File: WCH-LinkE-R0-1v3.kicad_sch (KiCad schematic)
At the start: 29 parts, among them Q1 IRLML2502TRPBF, Q2 IRLML2502TRPBF, SW1 PTS636_SL43_SMTR_LFS, SW2 PTS636_SL43_SMTR_LFS, SW3 PTS636_SL43_SMTR_LFS, U4 CH32V305FBP6, Y1 Crystal_GND24

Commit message: Improve layout
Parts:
- Q1, Q2: footprint Package_TO_SOT_SMD:SOT-23 -> Tiny_Scarab:SOT-23
- renumbered C13 to C12, C12 to C13, C14 to C15, C14 to C18, C14 to C19, D5 to D4, D4 to D5, R13 to R11, R13 to R14, R16 to R15, R11 to R16, R2 to R17, R3 to R18, R2 to R19, R1 to R20, R13 to R4, R14 to R5, R15 to R6, R8 to R7
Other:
- note added: "Mode LEDs"
- note added: "RST and IAP Buttons"
- note added: "The CH32V305FBP6 MCU outputs the LED_CON signal to indicate if it works in ARM-mode or RISC-V-mode."
- note added: "The RST button resets the CH32V305FBP6 MCU, the IAP button brings it into IAP mode."
- note removed: "The USB4110-GF-A USB-C connector only provides the basic USB2.0 data signals. We fuse the incoming VBUS supply at 1A."
- moved on the sheet: C14, C15, D4, D5, R15, R16, R17, R18, R19, R20, SW2, SW3

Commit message: Improve layout
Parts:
- added C18: 10u, Capacitor_SMD:C_0805_2012Metric, symbol Device:C
- added C21: 100n, Capacitor_SMD:C_0402_1005Metric_Pad0.74x0.62mm_HandSolder, symbol Device:C
- added R5, R7: 0, Resistor_SMD:R_0402_1005Metric_Pad0.72x0.64mm_HandSolder, symbol Device:R
- C19: renamed from C18; GPN GPC0402104-25 -> (none); MPN (none) -> GPC0402104-25
- C20: renamed from C19; GPN GPC0402104-25 -> (none); MPN (none) -> GPC0402104-25
- C22: renamed from C14; GPN GPC0402104-25 -> (none); MPN (none) -> GPC0402104-25
- C23: renamed from C15; GPN GPC0402104-25 -> (none); MPN (none) -> GPC0402104-25
- C24: renamed from C12; GPN GPC0402220 -> (none); MPN (none) -> GPC0402220; now left out of the parts list
- C25: renamed from C13; GPN GPC0402220 -> (none); MPN (none) -> GPC0402220; now left out of the parts list
- LED2: renamed from D4; MPN 150060GS55040 -> 150060YS55040; SPN 732-12014-2-ND -> 732-12018-2-ND
- LED3: renamed from D5; MPN 150060GS55040 -> 150060BS55040; SPN 732-12014-2-ND -> 732-12013-2-ND
- Q1, Q2: DPN IRLML2502TRPBFTR-ND -> (none); Distributor DigiKey -> (none); SPN (none) -> IRLML2502TRPBFTR-ND; Supplier (none) -> DigiKey
- R10: renamed from R14; GPN GPR04021K -> (none); MPN (none) -> GPR04021K
- R11: renamed from R17; GPN GPR0402100K -> (none); MPN (none) -> GPR0402100K
- R12: renamed from R18; GPN GPR04021K -> (none); MPN (none) -> GPR04021K
- R13: renamed from R19; value 300 -> 130; GPN GPR0402300R -> (none); MPN (none) -> GPR0402130R
- R14: renamed from R20; value 75 -> 20; GPN GPR040275R -> (none); MPN (none) -> GPR040220R
- R15, R16: GPN GPR040210K -> (none); MPN (none) -> GPR040210K
- R17: renamed from R6; GPN GPR04020R -> (none); MPN (none) -> GPR04020R
- R18: renamed from R4; GPN GPR04020R -> (none); MPN (none) -> GPR04020R
- R19: renamed from R5; GPN GPR04020R -> (none); MPN (none) -> GPR04020R
- R4: renamed from R9; GPN GPR0402270R -> (none); MPN (none) -> GPR0402270R
- R6: renamed from R10; GPN GPR0402270R -> (none); MPN (none) -> GPR0402270R
- R8: renamed from R11; GPN GPR04020R -> (none); MPN (none) -> GPR04020R
- R9: renamed from R7; GPN GPR0402100R -> (none); MPN (none) -> GPR0402100R; now left out of the parts list
- U2: renamed from U4; now not fitted; now left out of the parts list
- renumbered SW2 to SW1, SW3 to SW2, SW1 to SW3, Y1 to XTAL1
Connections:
- net +3V3: now also C18.1, C21.1
- net GND: now also C18.2, C21.2
- net UART3_RX: now also R7.2; no longer U2.4 (PB11)
- net UART3_TX: now also R5.2; no longer U2.3 (PB10)
- new net: R5.1, U2.3 (PB10)
- new net: R7.1, U2.4 (PB11)
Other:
- note added: "10mA 1V95 YELLOW"
- note added: "10mA 3V10 BLUE"
- note removed: "5mA 1V7 AMBER"
- note removed: "5mA 2V9 BLUE"
- moved on the sheet: C19, C20, R4, R6, R8

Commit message: Update design
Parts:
- R5, R7: value 0 -> 270; MPN GPR02010R -> GPR0402270R; now not fitted; now left out of the parts list
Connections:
- net RX: now also R7.1
- net TX: now also R5.1
- net at U2.3 (PB10): now also R4.2, R7.2; no longer R5.1
- net at U2.4 (PB11): now also R5.2, R6.2; no longer R7.1
- removed net UART3_RX: R6.2, R7.2
- removed net UART3_TX: R4.2, R5.2
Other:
- moved on the sheet: R4, R6, R8

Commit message: Update layout
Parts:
- LED2, LED3: value LED -> ~
- Q1, Q2: value IRLML2502TRPBF -> ~
- SW2, SW3: value PTS636_SL43_SMTR_LFS -> ~
- U2: value CH32V305FBP6 -> ~; MPN (none) -> CH32V305FBP6; Manufacturer (none) -> WCH; SPN (none) -> 1005004329064488; Supplier (none) -> AliExpress; now fitted; now in the parts list
- XTAL1: value Crystal_GND24 -> (none)
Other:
- note added: "The CH32V305FBP6 is the heart of the WCH-LinkE-R0-1v3 on-board probe. It must be flashed through signals SWDIO_IN, SWDIO_IN and RST_IN. From then onwards, it gets its instructions from the USB signals USB_N and USB_P. It outputs the following signals to flash and debug the target MCU: - SWDIO_OUT - RST_OUT - TX - RX Note: Resistor R9 must be mounted after flashing the CH32V305FBP6 MCU."
- note removed: "The CH32V305FBP6 is the heart of the WCH-LinkE-R0-1v3 on-board probe. It must be flashed through signals SWDIO_IN, SWDIO_IN and RST_IN. From then onwards, it gets its instructions from the USB signals USB_N and USB_P. It outputs the following signals to flash and debug the target MCU: - SWDIO_OUT - RST_OUT - TX - RX Note: Resistor R7 must be mounted after flashing the CH32V305FBP6 MCU."
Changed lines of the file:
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@@
     (effects (font (size 1.27 1.27)) (justify left bottom))
   )
-  (text "The CH32V305FBP6 is the heart of the WCH-LinkE-R0-1v3\non-board probe. It must be flashed through signals\nSWDIO_IN, SWDIO_IN and RST_IN.\n\nFrom then onwards, it gets its instructions from the USB\nsignals USB_N and USB_P.\n\nIt outputs the following signals to flash and debug the\ntarget MCU:\n- SWDIO_OUT\n- RST_OUT\n- TX\n- RX\n\nNote: Resistor R7 must be mounted after\nflashing the CH32V305FBP6 MCU."
+  (text "The CH32V305FBP6 is the heart of the WCH-LinkE-R0-1v3\non-board probe. It must be flashed through signals\nSWDIO_IN, SWDIO_IN and RST_IN.\n\nFrom then onwards, it gets its instructions from the USB\nsignals USB_N and USB_P.\n\nIt outputs the following signals to flash and debug the\ntarget MCU:\n- SWDIO_OUT\n- RST_OUT\n- TX\n- RX\n\nNote: Resistor R9 must be mounted after\nflashing the CH32V305FBP6 MCU."
     (at 58.42 57.15 0)
     (effects (font (size 1.27 1.27)) (justify left bottom))
@@
       (effects (font (size 1.27 1.27)) (justify left))
     )
-    (property "Value" "IRLML2502TRPBF" (at 55.88 114.3 0)
+    (property "Value" "~" (at 55.88 114.3 0)
       (effects (font (size 1.27 1.27)) (justify left) hide)
     )
@@
       (effects (font (size 1.27 1.27)) (justify right))
     )
-    (property "Value" "LED" (at 43.18 95.25 90)
+    (property "Value" "~" (at 43.18 95.25 90)
       (effects (font (size 1.27 1.27)) (justify right) hide)
     )
@@
       (effects (font (size 1.27 1.27)) (justify left))
     )
-    (property "Value" "PTS636_SL43_SMTR_LFS" (at 113.03 90.17 0)
+    (property "Value" "~" (at 113.03 90.17 0)
       (effects (font (size 1.27 1.27)) hide)
     )
@@
       (effects (font (size 1.27 1.27)) (justify right))
     )
-    (property "Value" "LED" (at 55.88 95.25 0)
+    (property "Value" "~" (at 55.88 95.25 0)
       (effects (font (size 1.27 1.27)) (justify right) hide)
     )
@@
   )
   (symbol (lib_id "Tiny_Scarab:CH32V305FBP6") (at 171.45 39.37 0) (unit 1)
-    (in_bom no) (on_board yes) (dnp yes)
+    (in_bom yes) (on_board yes) (dnp no)
     (property "Reference" "U2" (at 180.34 22.86 0)
       (effects (font (size 1.27 1.27)))
     )
-    (property "Value" "CH32V305FBP6" (at 168.91 22.86 0)
-      (effects (font (size 1.27 1.27)))
+    (property "Value" "~" (at 168.91 22.86 0)
+      (effects (font (size 1.27 1.27)) hide)
     )
     (property "Footprint" "Package_SO:TSSOP-20_4.4x6.5mm_P0.65mm" (at 172.72 69.85 0)
@@
     )
     (property "Datasheet" "" (at 175.26 50.8 0)
+      (effects (font (size 1.27 1.27)) hide)
+    )
+    (property "Manufacturer" "WCH" (at 171.45 39.37 0)
+      (effects (font (size 1.27 1.27)) hide)
+    )
+    (property "MPN" "CH32V305FBP6" (at 168.91 22.86 0)
+      (effects (font (size 1.27 1.27)))
+    )
+    (property "Supplier" "AliExpress" (at 171.45 39.37 0)
+      (effects (font (size 1.27 1.27)) hide)
+    )
+    (property "SPN" "1005004329064488" (at 171.45 39.37 0)
       (effects (font (size 1.27 1.27)) hide)
     )
@@
       (effects (font (size 1.27 1.27)) (justify left))
     )
-    (property "Value" "PTS636_SL43_SMTR_LFS" (at 157.48 91.44 0)
+    (property "Value" "~" (at 157.48 91.44 0)
       (effects (font (size 1.27 1.27)) hide)
     )
@@
       (effects (font (size 1.27 1.27)))
     )
-    (property "Value" "Crystal_GND24" (at 146.05 95.25 90)
+    (property "Value" "" (at 146.05 95.25 90)
       (effects (font (size 1.27 1.27)) hide)
     )
@@
       (effects (font (size 1.27 1.27)) (justify left))
     )
-    (property "Value" "IRLML2502TRPBF" (at 44.45 114.3 0)
+    (property "Value" "~" (at 44.45 114.3 0)
       (effects (font (size 1.27 1.27)) (justify left) hide)
     )

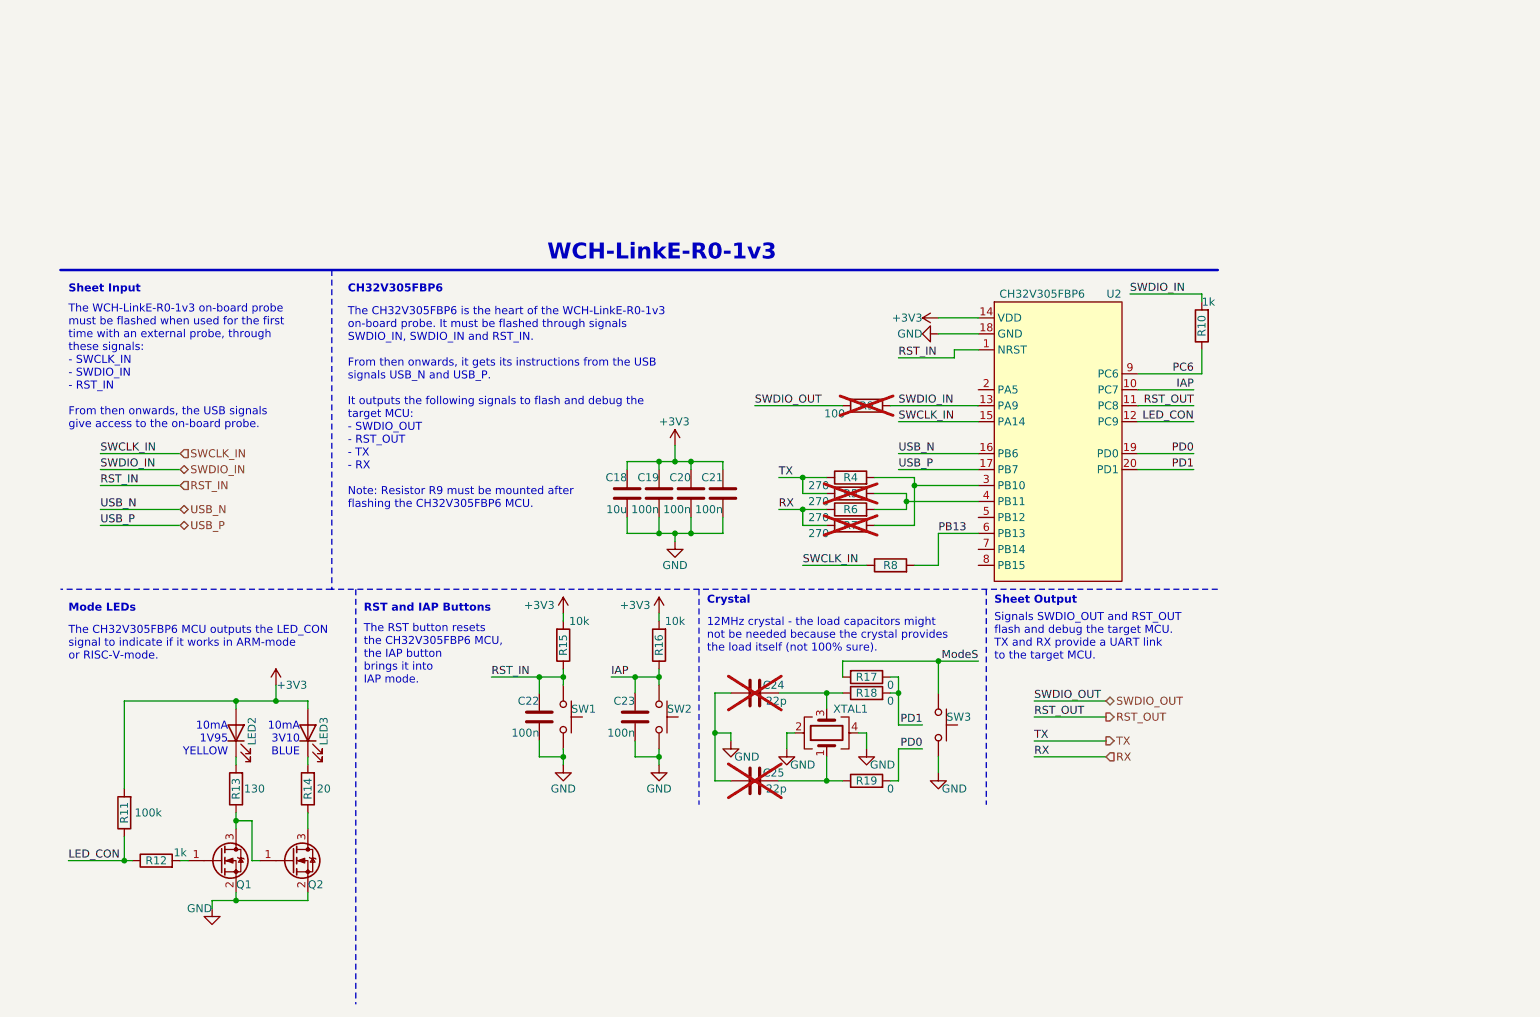
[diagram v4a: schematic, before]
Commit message: Prepare PCB for JLCPCB production
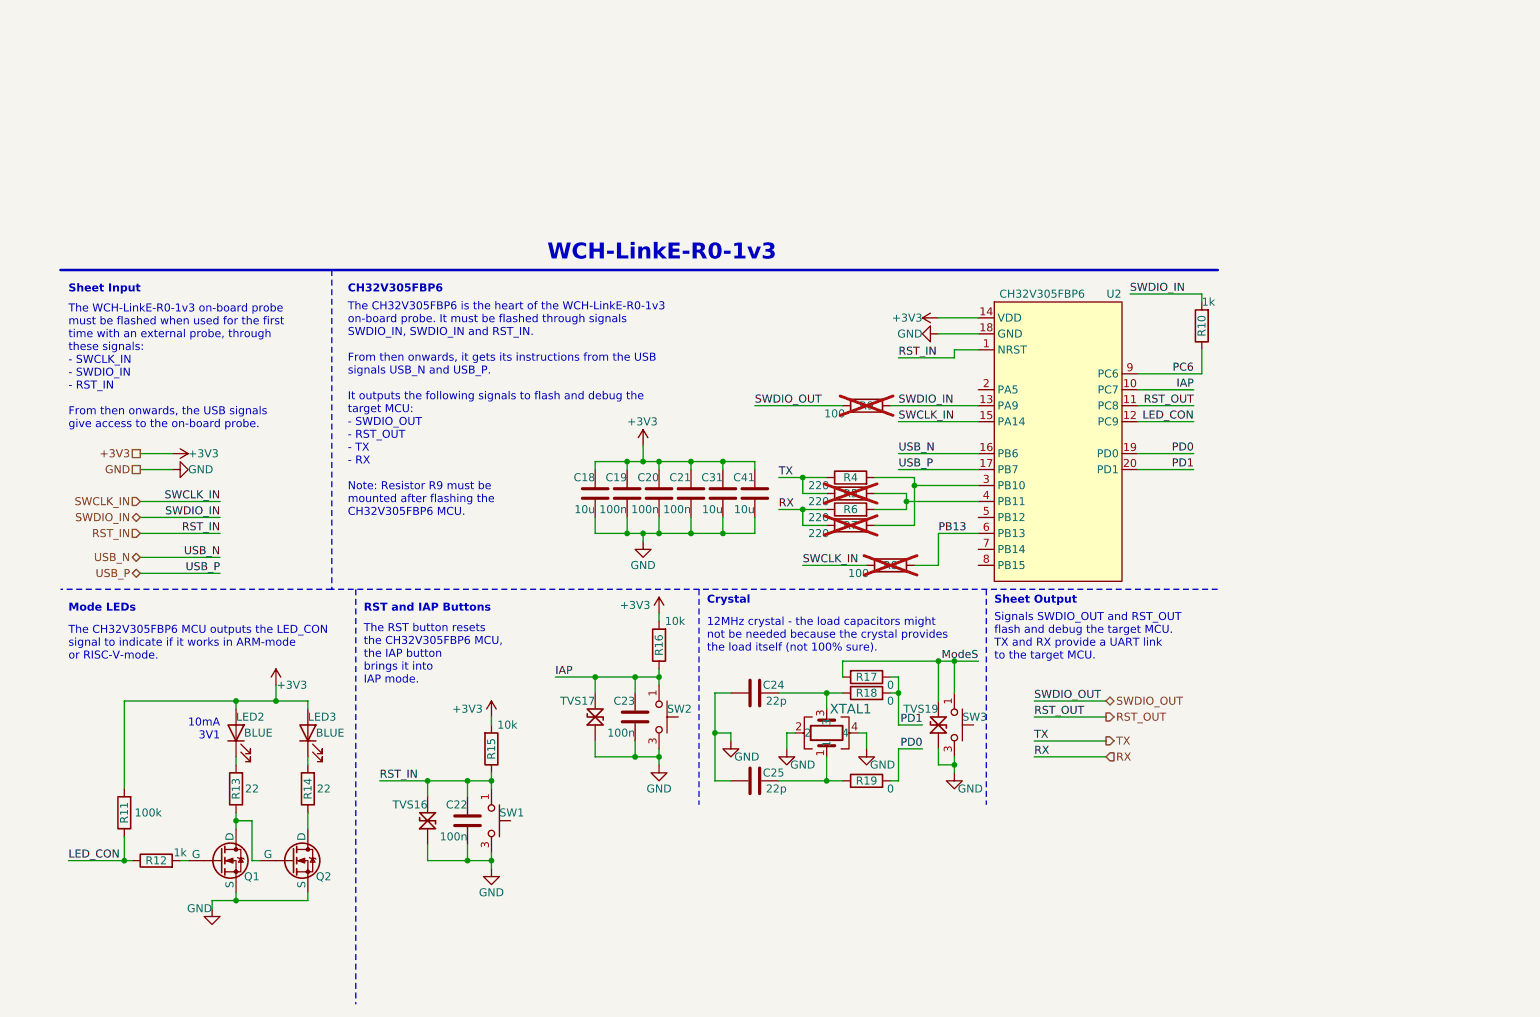
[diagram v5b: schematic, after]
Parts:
- removed LED2, LED3: ~, LED_SMD:LED_0603_1608Metric_Pad1.05x0.95mm_HandSolder, symbol Device:LED
- removed Q1, Q2: ~, Tiny_Scarab:SOT-23, symbol Tiny_Scarab:IRLML2502TRPBF
- removed SW1: PTS636_SL43_SMTR_LFS, Tiny_Scarab:SW_Tactile_SPST_NO_Straight_CK_PTS636Sx43SMTRLFS, symbol Tiny_Scarab:PTS636_SL43_SMTR_LFS
- removed SW2, SW3: ~, Tiny_Scarab:SW_Tactile_SPST_NO_Straight_CK_PTS636Sx43SMTRLFS, symbol Tiny_Scarab:PTS636_SL43_SMTR_LFS
- removed XTAL1: (no value), Crystal:Crystal_SMD_3225-4Pin_3.2x2.5mm, symbol Device:Crystal_GND24
- added C31, C41: 10u, Capacitor_SMD:C_0805_2012Metric, symbol Device:C
- added LED2, LED3: BLUE, Tiny_Scarab:LED_0603_CSL0902BT, symbol Tiny_Scarab:LED_BLUE_CSL0902BT
- added Q1, Q2: DMG1012UW-7, Tiny_Scarab:SOT-323_SC-70, symbol Tiny_Scarab:NMOS_DMG1012UW-7
- added SW1, SW2, SW3: SKRPASE010, Tiny_Scarab:SW_Tactile_SPST_NO_Straight_ALPSALPINE_SKRP, symbol Tiny_Scarab:SKRPASE010
- added TVS16, TVS17, TVS19: 5V, Tiny_Scarab:D_SOD-323_CDSOD323-T05LC, symbol Tiny_Scarab:CDSOD323-T05LC
- added XTAL1: SX5B12.000F2020F30, Tiny_Scarab:CRYSTAL-SMD5032-4P, symbol Tiny_Scarab:SX5B12.000F2020F30
- C18: JLCPCB Part # (none) -> C15850; MPN GPC0805106 -> CL21A106KAYNNNE; Manufacturer (none) -> Samsung electro-mechanics
- C19, C20, C21, C22, C23: JLCPCB Part # (none) -> C1525; MPN GPC0402104-25 -> CL05B104KO5NNNC; Manufacturer (none) -> Samsung electro-mechanics
- C24, C25: JLCPCB Part # (none) -> C1555; MPN GPC0402220 -> 0402CG220J500NT; Manufacturer (none) -> FH (Guangdong Fenghua Advanced Tech); now fitted; now in the parts list
- R10, R12: JLCPCB Part # (none) -> C11702; MPN GPR04021K -> 0402WGF1001TCE; Manufacturer (none) -> UNI-ROYAL(Uniroyal Elec)
- R11: JLCPCB Part # (none) -> C25741; MPN GPR0402100K -> 0402WGF1003TCE; Manufacturer (none) -> UNI-ROYAL(Uniroyal Elec)
- R13: value 130 -> 22; JLCPCB Part # (none) -> C25092; MPN GPR0402130R -> 0402WGF220JTCE; Manufacturer (none) -> UNI-ROYAL(Uniroyal Elec)
- R14: value 20 -> 22; JLCPCB Part # (none) -> C25092; MPN GPR040220R -> 0402WGF220JTCE; Manufacturer (none) -> UNI-ROYAL(Uniroyal Elec)
- R15, R16: JLCPCB Part # (none) -> C25744; MPN GPR040210K -> 0402WGF1002TCE; Manufacturer (none) -> UNI-ROYAL(Uniroyal Elec)
- R17, R18, R19: JLCPCB Part # (none) -> C17168; MPN GPR04020R -> 0402WGF0000TCE; Manufacturer (none) -> UNI-ROYAL(Uniroyal Elec)
- R4, R5, R6, R7: value 270 -> 220; JLCPCB Part # (none) -> C25091; MPN GPR0402270R -> 0402WGF2200TCE; Manufacturer (none) -> UNI-ROYAL(Uniroyal Elec)
- R8: value 0 -> 100; JLCPCB Part # (none) -> C25076; MPN GPR04020R -> 0402WGF1000TCE; Manufacturer (none) -> UNI-ROYAL(Uniroyal Elec); now not fitted; now left out of the parts list
- R9: JLCPCB Part # (none) -> C25076; MPN GPR0402100R -> 0402WGF1000TCE; Manufacturer (none) -> UNI-ROYAL(Uniroyal Elec)
- U2: JLCPCB Part # (none) -> C5123443
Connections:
- net +3V3: now also C31.1, C41.1, LED2.2 (A), LED3.2 (A)
- net GND: now also C31.2, C41.2, Q1.2 (S), Q2.2 (S), SW1.3, SW1.4, SW2.3, SW2.4, SW3.3, SW3.4, TVS16.2, TVS17.2, TVS19.2, XTAL1.2, XTAL1.4
- net IAP: now also SW2.1, SW2.2, TVS17.1
- net ModeS: now also SW3.1, SW3.2, TVS19.1
- net RST_IN: now also SW1.1, SW1.2, TVS16.1
- net at R13.1: now also Q1.3 (D), Q2.1 (G)
- net at R14.1: now also Q2.3 (D)
- net at R13.2: now also LED2.1 (K)
- net at R14.2: now also LED3.1 (K)
- net at C24.2, R18.1: now also XTAL1.3
- net at C25.2, R19.1: now also XTAL1.1
- net at R12.2: now also Q1.1 (G)
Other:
- note added: "10mA 3V1"
- note removed: "10mA 1V95 YELLOW"
- note removed: "10mA 3V10 BLUE"
- moved on the sheet: C18, C19, C20, C21, C22, R15

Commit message: Renumber designators and draw new silkscreen
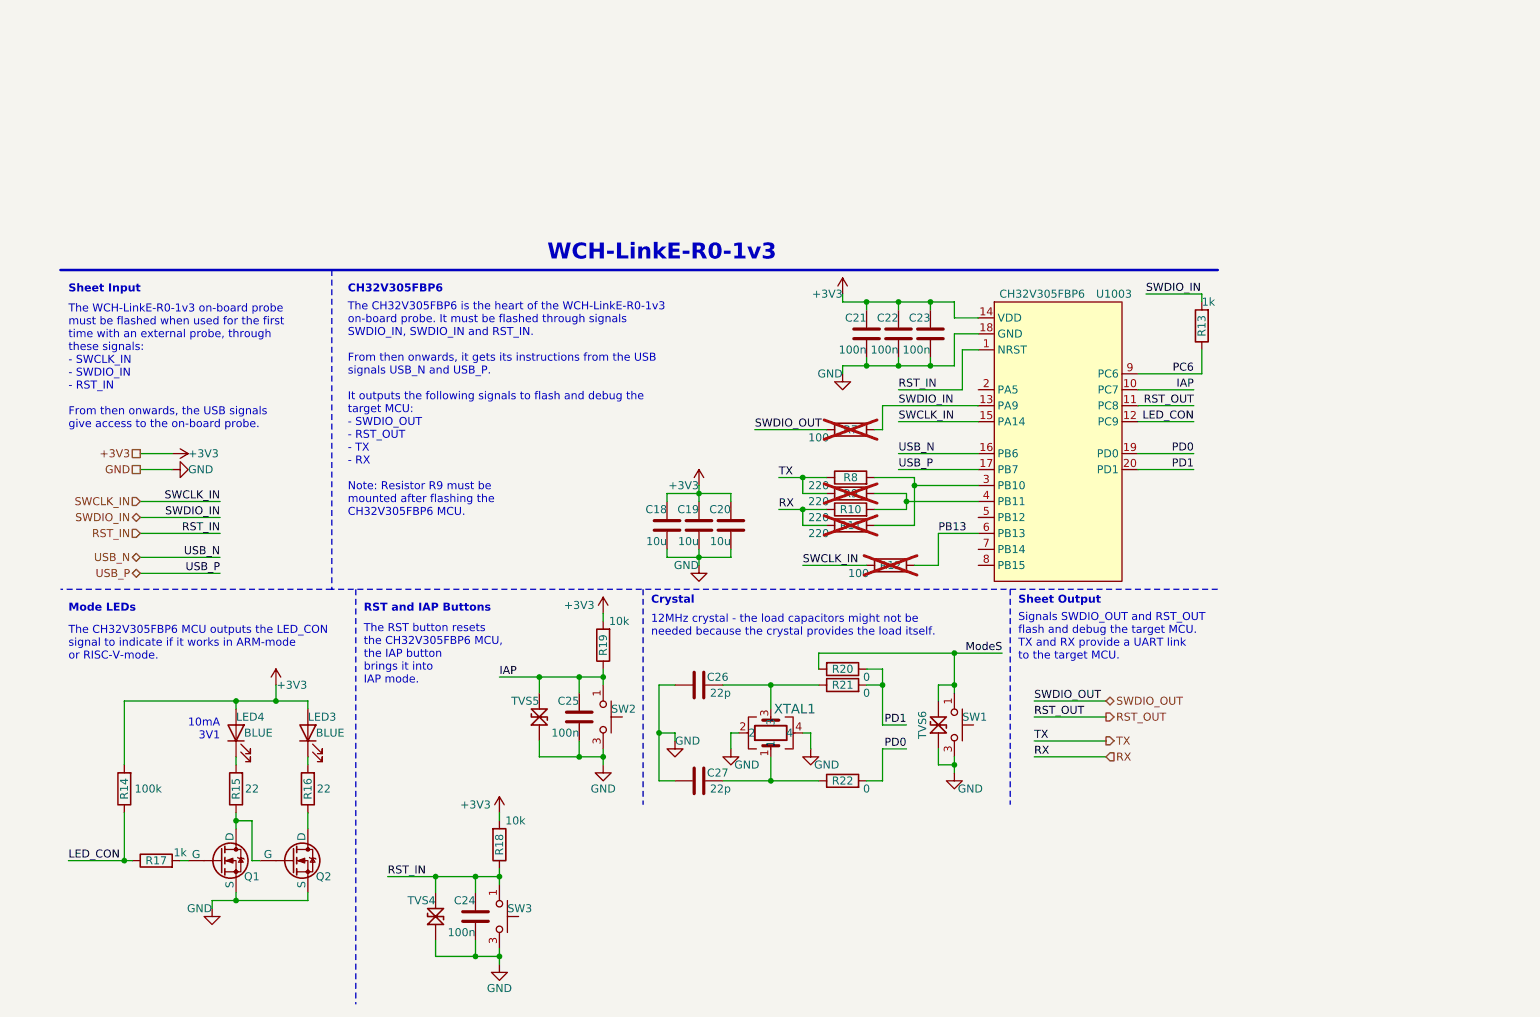
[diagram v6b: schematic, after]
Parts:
- renumbered C31 to C19, C41 to C20, C20 to C22, C19 to C23, C22 to C24, C23 to C25, C24 to C26, C25 to C27, LED2 to LED4, R6 to R10, R7 to R11, R8 to R12, R10 to R13, R11 to R14, R13 to R15, R14 to R16, R12 to R17, R15 to R18, R16 to R19, R17 to R20, R18 to R21, R19 to R22, R9 to R7, R4 to R8, R5 to R9, SW3 to SW1, SW1 to SW3, TVS16 to TVS4, TVS17 to TVS5, TVS19 to TVS6, U2 to U1003
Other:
- note added: "12MHz crystal - the load capacitors might not be needed because the crystal provides the load itself."
- note removed: "12MHz crystal - the load capacitors might not be needed because the crystal provides the load itself (not 100% sure)."
- moved on the sheet: C18, C19, C20, C21, C22, C23, C24, C25, C26, C27, R14, R18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
